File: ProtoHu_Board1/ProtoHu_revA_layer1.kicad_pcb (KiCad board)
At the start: 2 copper layers, 54 x 85.6 mm, 8 parts, among them IC1 SST39SF040-45-4C-WHE-T, IC2 74LS32, J1 HUCARD-EDGE, J2 SST39SF040-70-4C-PHE

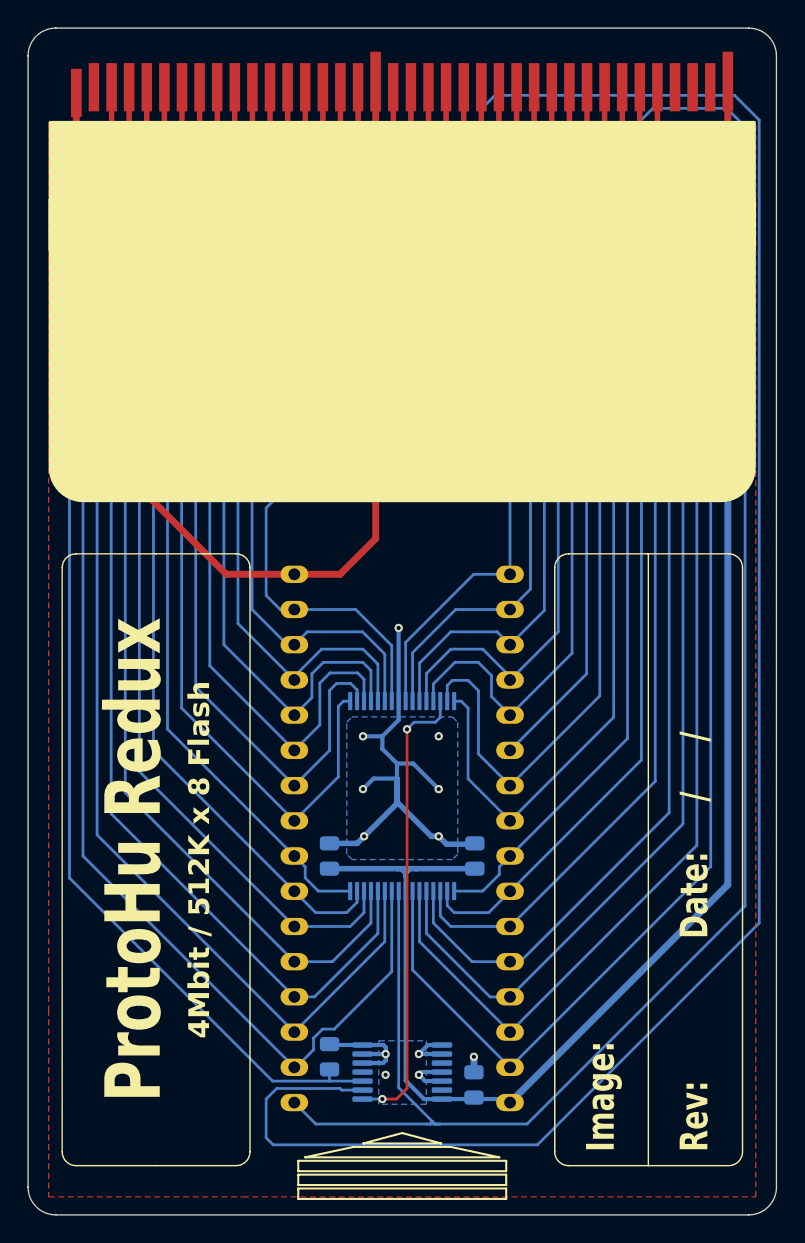
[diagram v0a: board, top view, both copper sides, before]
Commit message: Fix pinout and part (LS -> HC) for IC2.
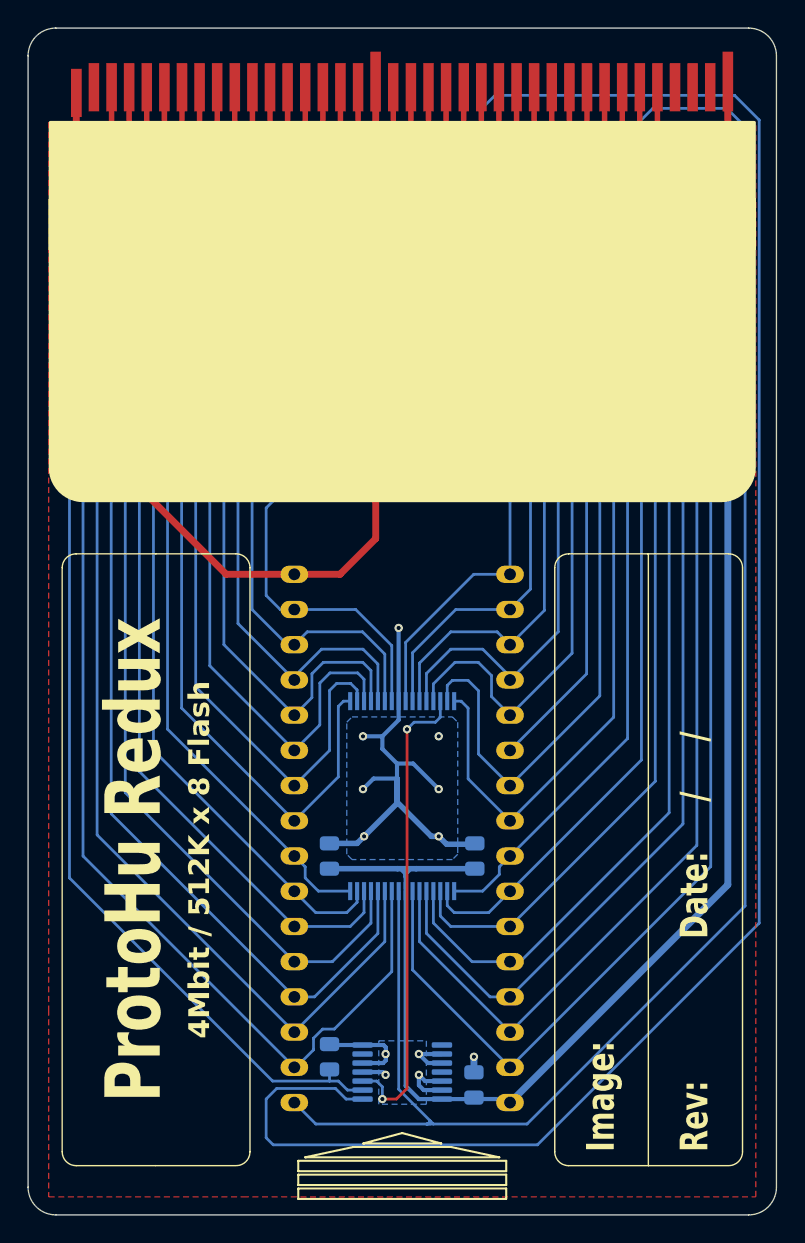
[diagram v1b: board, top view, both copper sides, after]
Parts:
- IC2: value 74LS32 -> 74HC32
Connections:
- IC2 pad 1: FLASH_CE -> A20
- IC2 pad 10: unconnected-(IC2-Pad10) -> GND
- IC2 pad 11: GND -> unconnected-(IC2-Pad11)
- IC2 pad 13: unconnected-(IC2-Pad13) -> GND
- IC2 pad 2: A20 -> A19
- IC2 pad 3: A19 -> FLASH_CE
- IC2 pad 4: unconnected-(IC2-Pad4) -> GND
- IC2 pad 6: GND -> unconnected-(IC2-Pad6)
- IC2 pad 8: GND -> unconnected-(IC2-Pad8)
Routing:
- net FLASH_CE: track 33.4 -> 34.4 mm
- net GND: track 137.0 -> 137.9 mm
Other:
- board text added: "1.6mm"

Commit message: Correct Board 1 thickness hint on silkscreen.
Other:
- board text added: "0.8mm"
- board text removed: "1.6mm"
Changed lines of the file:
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@@
     (effects (font (size 1 1) (thickness 0.1)) (justify mirror))
   )
-  (gr_text "1.6mm" (at 148.45 79.7) (layer "B.SilkS")
+  (gr_text "0.8mm" (at 148.45 79.7) (layer "B.SilkS")
     (effects (font (size 1.5 1.5) (thickness 0.3) bold) (justify mirror))
   )
